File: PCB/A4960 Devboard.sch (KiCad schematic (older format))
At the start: 61 parts, among them IC1 ATMEGA8-AI, P1 CONN_02X03, P2 CONN_01X02, P3 CONN_01X03, P4 CONN_01X03, Q1 Q_NMOS_GDS, Q2 Q_NMOS_GDS, Q3 Q_NMOS_GDS, Q4 Q_NMOS_GDS, Q5 Q_NMOS_GDS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

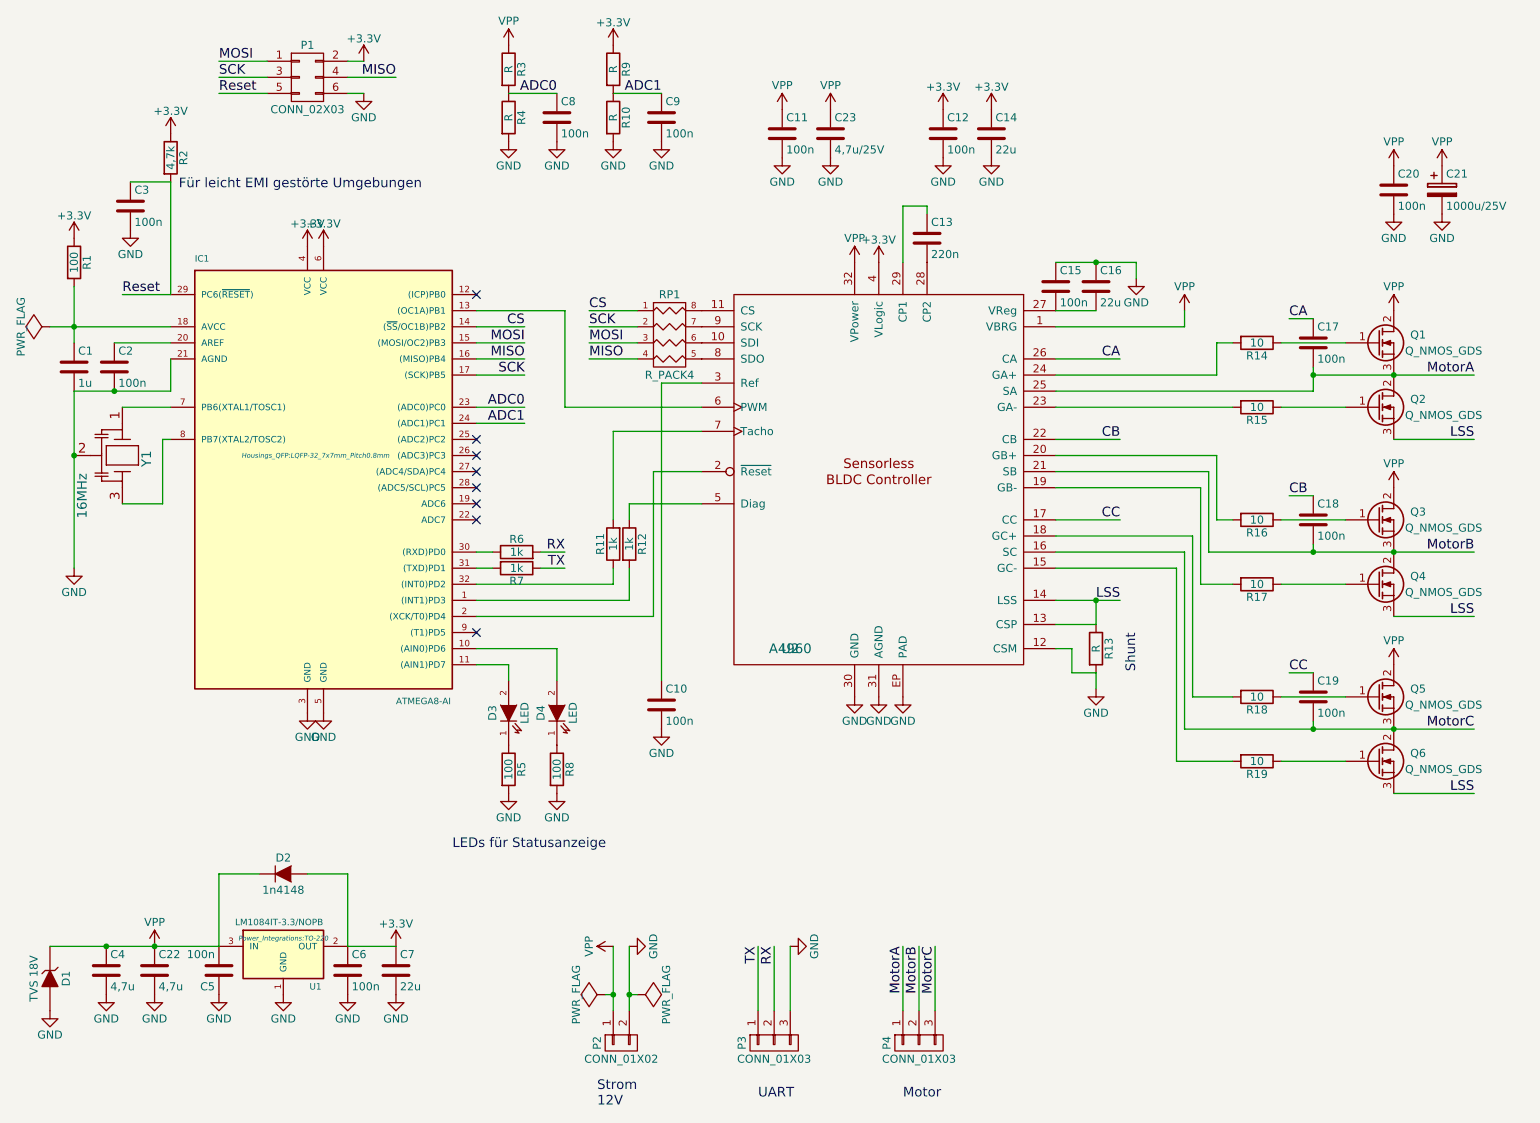
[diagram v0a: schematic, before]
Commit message: Library-Refferenz geändert & Layout: Vcc von 3.3V auf 5V
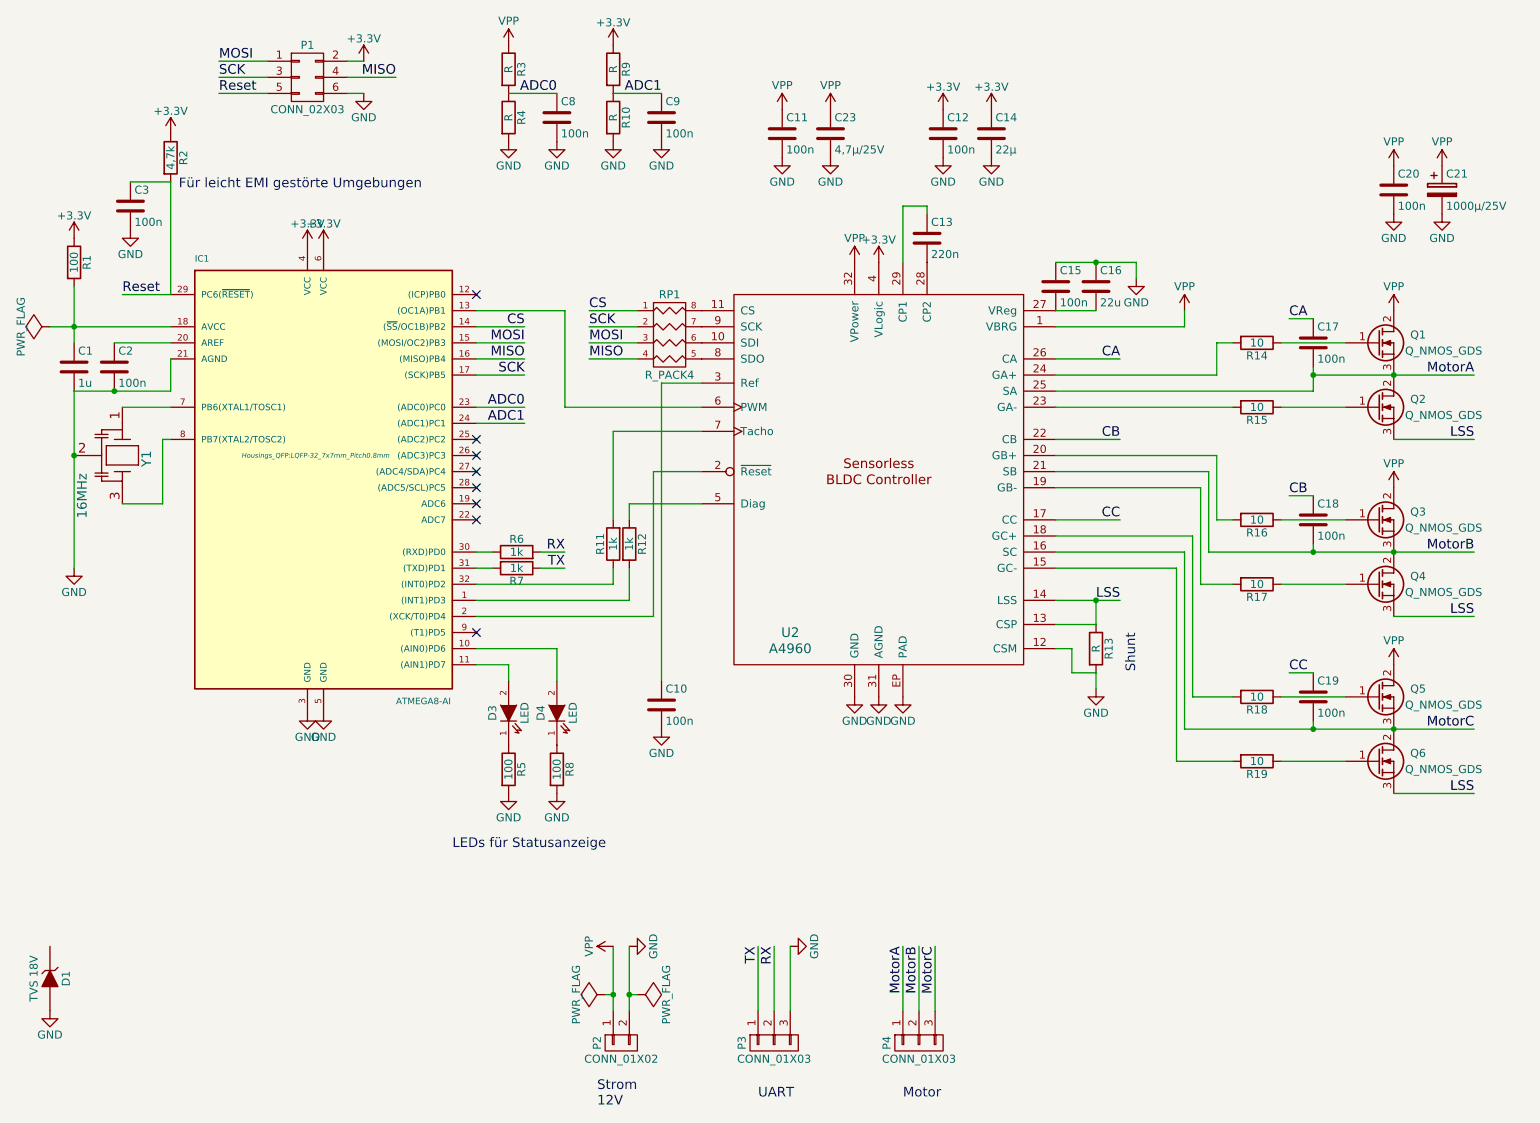
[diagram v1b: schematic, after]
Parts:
- removed C22, C4: 4,7u, Capacitors_SMD:C_1206, symbol C
- removed C5, C6: 100n, Capacitors_SMD:C_0603, symbol C
- removed C7: 22u, Capacitors_SMD:C_1206, symbol C
- removed D2: 1n4148, Diodes_SMD:MiniMELF_Standard, symbol D
- removed U1: LM1084IT-3.3/NOPB, Power_Integrations:TO-220, symbol LM1084IT-3.3/NOPB
- C14: value 22u -> 22µ
- C21: value 1000u/25V -> 1000µ/25V
- C23: value 4,7u/25V -> 4,7µ/25V
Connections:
- net VPP: no longer D1.1 (K)
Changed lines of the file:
@@
 U 1 1 55EC77AA
 P 5950 3550
-F 0 "U2" H 5400 2500 60  0000 C CNN
+F 0 "U2" H 5400 2600 60  0000 C CNN
 F 1 "A4960" H 5400 2500 60  0000 C CNN
 F 2 "Housings_QFP:TQFP-32_7x7mm_Pitch0.8mm" H 5400 2500 60  0001 C CNN
@@
 P 6650 1400
 F 0 "C14" H 6675 1500 50  0000 L CNN
-F 1 "22u" H 6675 1300 50  0000 L CNN
+F 1 "22µ" H 6675 1300 50  0000 L CNN
 F 2 "Capacitors_SMD:C_1206" H 6688 1250 30  0001 C CNN
 F 3 "" H 6650 1400 60  0000 C CNN
@@
 P 9450 1750
 F 0 "C21" H 9475 1850 50  0000 L CNN
-F 1 "1000u/25V" H 9475 1650 50  0000 L CNN
+F 1 "1000µ/25V" H 9475 1650 50  0000 L CNN
 F 2 "" H 9488 1600 30  0001 C CNN
 F 3 "" H 9450 1750 60  0000 C CNN
@@
 LEDs für Statusanzeige
 $Comp
-L LM1084IT-3.3/NOPB U1
-U 1 1 55ECD83D
-P 2250 6500
-F 0 "U1" H 2450 6300 40  0000 C CNN
-F 1 "LM1084IT-3.3/NOPB" H 1950 6700 40  0000 L CNN
-F 2 "Power_Integrations:TO-220" H 2250 6600 30  0000 C CIN
-F 3 "" H 2250 6500 60  0000 C CNN
-	1    2250 6500
-	1    0    0    -1
-$EndComp
-$Comp
-L C C5
-U 1 1 55ECDA89
-P 1850 6600
-F 0 "C5" H 1875 6700 50  0000 L CNN
-F 1 "100n" H 1875 6500 50  0000 L CNN
-F 2 "Capacitors_SMD:C_0603" H 1888 6450 30  0001 C CNN
-F 3 "" H 1850 6600 60  0000 C CNN
-	1    1850 6600
-	-1   0    0    1
-$EndComp
-$Comp
-L C C6
-U 1 1 55ECDC37
-P 2650 6600
-F 0 "C6" H 2675 6700 50  0000 L CNN
-F 1 "100n" H 2675 6500 50  0000 L CNN
-F 2 "Capacitors_SMD:C_0603" H 2688 6450 30  0001 C CNN
-F 3 "" H 2650 6600 60  0000 C CNN
-	1    2650 6600
-	1    0    0    -1
-$EndComp
-$Comp
-L C C7
-U 1 1 55ECDE0F
-P 2950 6600
-F 0 "C7" H 2975 6700 50  0000 L CNN
-F 1 "22u" H 2975 6500 50  0000 L CNN
-F 2 "Capacitors_SMD:C_1206" H 2988 6450 30  0001 C CNN
-F 3 "" H 2950 6600 60  0000 C CNN
-	1    2950 6600
-	1    0    0    -1
-$EndComp
-$Comp
-L GND #PWR040
-U 1 1 55ECE074
-P 1450 6750
-F 0 "#PWR040" H 1450 6500 50  0001 C CNN
-F 1 "GND" H 1450 6600 50  0000 C CNN
-F 2 "" H 1450 6750 60  0000 C CNN
-F 3 "" H 1450 6750 60  0000 C CNN
-	1    1450 6750
-	1    0    0    -1
-$EndComp
-$Comp
-L GND #PWR041
-U 1 1 55ECE11E
-P 1850 6750
-F 0 "#PWR041" H 1850 6500 50  0001 C CNN
-F 1 "GND" H 1850 6600 50  0000 C CNN
-F 2 "" H 1850 6750 60  0000 C CNN
-F 3 "" H 1850 6750 60  0000 C CNN
-	1    1850 6750
-	1    0    0    -1
-$EndComp
-$Comp
-L GND #PWR042
-U 1 1 55ECE1C8
-P 2250 6750
-F 0 "#PWR042" H 2250 6500 50  0001 C CNN
-F 1 "GND" H 2250 6600 50  0000 C CNN
-F 2 "" H 2250 6750 60  0000 C CNN
-F 3 "" H 2250 6750 60  0000 C CNN
-	1    2250 6750
-	1    0    0    -1
-$EndComp
-$Comp
-L GND #PWR043
-U 1 1 55ECE272
-P 2650 6750
-F 0 "#PWR043" H 2650 6500 50  0001 C CNN
-F 1 "GND" H 2650 6600 50  0000 C CNN
-F 2 "" H 2650 6750 60  0000 C CNN
-F 3 "" H 2650 6750 60  0000 C CNN
-	1    2650 6750
-	1    0    0    -1
-$EndComp
-$Comp
-L GND #PWR044
-U 1 1 55ECE31C
-P 2950 6750
-F 0 "#PWR044" H 2950 6500 50  0001 C CNN
-F 1 "GND" H 2950 6600 50  0000 C CNN
-F 2 "" H 2950 6750 60  0000 C CNN
-F 3 "" H 2950 6750 60  0000 C CNN
-	1    2950 6750
-	1    0    0    -1
-$EndComp
-$Comp
 L ZENER D1
 U 1 1 55ECE4C5
@@
 	1    0    0    -1
 $EndComp
-Wire Wire Line
-	800  6450 1850 6450
-Connection ~ 1450 6450
-Wire Wire Line
-	2650 6450 2950 6450
-$Comp
-L +3.3V #PWR046
-U 1 1 55ECE8BB
-P 2950 6450
-F 0 "#PWR046" H 2950 6300 50  0001 C CNN
-F 1 "+3.3V" H 2950 6590 50  0000 C CNN
-F 2 "" H 2950 6450 60  0000 C CNN
-F 3 "" H 2950 6450 60  0000 C CNN
-	1    2950 6450
-	1    0    0    -1
-$EndComp
-$Comp
-L D D2
-U 1 1 55ECE9B8
-P 2250 6000
-F 0 "D2" H 2250 6100 50  0000 C CNN
-F 1 "1n4148" H 2250 5900 50  0000 C CNN
-F 2 "Diodes_SMD:MiniMELF_Standard" H 2250 6000 60  0001 C CNN
-F 3 "" H 2250 6000 60  0000 C CNN
-	1    2250 6000
-	1    0    0    -1
-$EndComp
-Wire Wire Line
-	2400 6000 2650 6000
-Wire Wire Line
-	2650 6000 2650 6450
-Wire Wire Line
-	2100 6000 1850 6000
-Wire Wire Line
-	1850 6000 1850 6450
 $Comp
 L CONN_01X03 P3
@@
 	4400 6450 4400 6850
 $Comp
-L VPP #PWR049
-U 1 1 55ED031C
-P 1450 6450
-F 0 "#PWR049" H 1450 6300 50  0001 C CNN
-F 1 "VPP" H 1450 6600 50  0000 C CNN
-F 2 "" H 1450 6450 60  0000 C CNN
-F 3 "" H 1450 6450 60  0000 C CNN
-	1    1450 6450
-	1    0    0    -1
-$EndComp
-$Comp
 L VPP #PWR050
 U 1 1 55ED0449
@@
 P 5650 1400
 F 0 "C23" H 5675 1500 50  0000 L CNN
-F 1 "4,7u/25V" H 5675 1300 50  0000 L CNN
+F 1 "4,7µ/25V" H 5675 1300 50  0000 L CNN
 F 2 "Capacitors_SMD:C_1206" H 5688 1250 30  0001 C CNN
 F 3 "" H 5650 1400 60  0000 C CNN
@@
 	1    0    0    -1
 $EndComp
-$Comp
-L C C22
-U 1 1 55ED2F02
-P 1450 6600
-F 0 "C22" H 1475 6700 50  0000 L CNN
-F 1 "4,7u" H 1475 6500 50  0000 L CNN
-F 2 "Capacitors_SMD:C_1206" H 1488 6450 30  0001 C CNN
-F 3 "" H 1450 6600 60  0000 C CNN
-F 4 "C1206C475K3RACTU" H 1450 6600 60  0001 C CNN "Herstellername"
-	1    1450 6600
-	1    0    0    -1
-$EndComp
-$Comp
-L C C4
-U 1 1 55ED3212
-P 1150 6600
-F 0 "C4" H 1175 6700 50  0000 L CNN
-F 1 "4,7u" H 1175 6500 50  0000 L CNN
-F 2 "Capacitors_SMD:C_1206" H 1188 6450 30  0001 C CNN
-F 3 "" H 1150 6600 60  0000 C CNN
-F 4 "C1206C475K3RACTU" H 1150 6600 60  0001 C CNN "Herstellername"
-	1    1150 6600
-	1    0    0    -1
-$EndComp
-$Comp
-L GND #PWR057
-U 1 1 55ED32E2
-P 1150 6750
-F 0 "#PWR057" H 1150 6500 50  0001 C CNN
-F 1 "GND" H 1150 6600 50  0000 C CNN
-F 2 "" H 1150 6750 60  0000 C CNN
-F 3 "" H 1150 6750 60  0000 C CNN
-	1    1150 6750
-	1    0    0    -1
-$EndComp
-Connection ~ 1150 6450
 $EndSCHEMATC

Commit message: Änderung der FETs auf Pinnamen GDS
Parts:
- removed Q1, Q2, Q3, Q4, Q5, Q6: Q_NMOS_GDS, Transistors_TO-220:TO-220_Neutral123_Vertical_LargePads, symbol Q_NMOS_GDS
- added Q1, Q2, Q3, Q4, Q5, Q6: Q_NMOS_GDS_old, sven:SO8_WITH_Heatpipes, symbol Q_NMOS_GDS_old
- added R20: 1, Resistors_SMD:R_0805, symbol R
- added U1: LM2931AZ-5.0, toni:SOT223_GND_VO_VI, symbol LM2931AZ-5.0
- C21: footprint (none) -> Capacitors_ThroughHole:C_Radial_D8_L11.5_P3.5
- D1: footprint (none) -> Diodes_SMD:SOD-123
- P1: footprint (none) -> Pin_Headers:Pin_Header_Straight_2x03
- P2: footprint (none) -> Pin_Headers:Pin_Header_Straight_1x02
- P3, P4: footprint (none) -> Pin_Headers:Pin_Header_Straight_1x03
- Y1: footprint (none) -> toni:CerOsc_3,2x1,3
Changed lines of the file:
@@
-$EndComp
-$Comp
-L Q_NMOS_GDS Q1
-U 1 1 55EC7821
-P 9050 2700
-F 0 "Q1" H 9350 2750 50  0000 R CNN
-F 1 "Q_NMOS_GDS" H 9700 2650 50  0000 R CNN
-F 2 "Transistors_TO-220:TO-220_Neutral123_Vertical_LargePads" H 9250 2800 29  0001 C CNN
-F 3 "" H 9050 2700 60  0000 C CNN
-	1    9050 2700
-	1    0    0    -1
-$EndComp
-$Comp
-L Q_NMOS_GDS Q2
-U 1 1 55EC798C
-P 9050 3100
-F 0 "Q2" H 9350 3150 50  0000 R CNN
-F 1 "Q_NMOS_GDS" H 9700 3050 50  0000 R CNN
-F 2 "Transistors_TO-220:TO-220_Neutral123_Vertical_LargePads" H 9250 3200 29  0001 C CNN
-F 3 "" H 9050 3100 60  0000 C CNN
-	1    9050 3100
-	1    0    0    -1
 $EndComp
 $Comp
@@
 $EndComp
 $Comp
-L Q_NMOS_GDS Q3
-U 1 1 55EC85FE
-P 9050 3800
-F 0 "Q3" H 9350 3850 50  0000 R CNN
-F 1 "Q_NMOS_GDS" H 9700 3750 50  0000 R CNN
-F 2 "Transistors_TO-220:TO-220_Neutral123_Vertical_LargePads" H 9250 3900 29  0001 C CNN
-F 3 "" H 9050 3800 60  0000 C CNN
-	1    9050 3800
-	1    0    0    -1
-$EndComp
-$Comp
-L Q_NMOS_GDS Q4
-U 1 1 55EC8604
-P 9050 4200
-F 0 "Q4" H 9350 4250 50  0000 R CNN
-F 1 "Q_NMOS_GDS" H 9700 4150 50  0000 R CNN
-F 2 "Transistors_TO-220:TO-220_Neutral123_Vertical_LargePads" H 9250 4300 29  0001 C CNN
-F 3 "" H 9050 4200 60  0000 C CNN
-	1    9050 4200
-	1    0    0    -1
-$EndComp
-$Comp
 L C C18
 U 1 1 55EC860A
@@
 $EndComp
 $Comp
-L Q_NMOS_GDS Q5
-U 1 1 55EC8730
-P 9050 4900
-F 0 "Q5" H 9350 4950 50  0000 R CNN
-F 1 "Q_NMOS_GDS" H 9700 4850 50  0000 R CNN
-F 2 "Transistors_TO-220:TO-220_Neutral123_Vertical_LargePads" H 9250 5000 29  0001 C CNN
-F 3 "" H 9050 4900 60  0000 C CNN
-	1    9050 4900
-	1    0    0    -1
-$EndComp
-$Comp
-L Q_NMOS_GDS Q6
-U 1 1 55EC8736
-P 9050 5300
-F 0 "Q6" H 9350 5350 50  0000 R CNN
-F 1 "Q_NMOS_GDS" H 9700 5250 50  0000 R CNN
-F 2 "Transistors_TO-220:TO-220_Neutral123_Vertical_LargePads" H 9250 5400 29  0001 C CNN
-F 3 "" H 9050 5300 60  0000 C CNN
-	1    9050 5300
-	1    0    0    -1
-$EndComp
-$Comp
 L C C19
 U 1 1 55EC873C
@@
 F 0 "C21" H 9475 1850 50  0000 L CNN
 F 1 "1000µ/25V" H 9475 1650 50  0000 L CNN
-F 2 "" H 9488 1600 30  0001 C CNN
+F 2 "Capacitors_ThroughHole:C_Radial_D8_L11.5_P3.5" H 9488 1600 30  0001 C CNN
 F 3 "" H 9450 1750 60  0000 C CNN
 	1    9450 1750
@@
 F 0 "Y1" H 1220 3600 60  0000 C CNN
 F 1 "16MHz" H 1450 3200 60  0000 C CNN
-F 2 "" H 1200 3400 60  0001 C CNN
+F 2 "toni:CerOsc_3,2x1,3" H 1200 3400 60  0001 C CNN
 F 3 "" H 1200 3400 60  0000 C CNN
 	1    1200 3400
@@
 F 0 "P1" H 2400 1250 50  0000 C CNN
 F 1 "CONN_02X03" H 2400 850 50  0000 C CNN
-F 2 "" H 2400 -150 60  0001 C CNN
+F 2 "Pin_Headers:Pin_Header_Straight_2x03" H 2400 -150 60  0001 C CNN
 F 3 "" H 2400 -150 60  0000 C CNN
 	1    2400 1050
@@
 F 0 "D1" H 800 6750 50  0000 C CNN
 F 1 "TVS 18V" H 800 6550 50  0000 C CNN
-F 2 "" H 800 6650 60  0001 C CNN
+F 2 "Diodes_SMD:SOD-123" H 800 6650 60  0001 C CNN
 F 3 "" H 800 6650 60  0000 C CNN
 	1    800  6650
@@
 F 0 "P3" H 5300 7250 50  0000 C CNN
 F 1 "CONN_01X03" V 5400 7050 50  0000 C CNN
-F 2 "" H 5300 7050 60  0001 C CNN
+F 2 "Pin_Headers:Pin_Header_Straight_1x03" H 5300 7050 60  0001 C CNN
 F 3 "" H 5300 7050 60  0000 C CNN
 	1    5300 7050
@@
 F 0 "P2" H 4350 7200 50  0000 C CNN
 F 1 "CONN_01X02" V 4450 7050 50  0000 C CNN
-F 2 "" H 4350 7050 60  0001 C CNN
+F 2 "Pin_Headers:Pin_Header_Straight_1x02" H 4350 7050 60  0001 C CNN
 F 3 "" H 4350 7050 60  0000 C CNN
 	1    4350 7050
@@
 F 0 "P4" H 6200 7250 50  0000 C CNN
 F 1 "CONN_01X03" V 6300 7050 50  0000 C CNN
-F 2 "" H 6200 7050 60  0001 C CNN
+F 2 "Pin_Headers:Pin_Header_Straight_1x03" H 6200 7050 60  0001 C CNN
 F 3 "" H 6200 7050 60  0000 C CNN
 	1    6200 7050
@@
 	1    0    0    -1
 $EndComp
+$Comp
+L LM2931AZ-5.0 U1
+U 1 1 5653AFAA
+P 2400 6725
+F 0 "U1" H 2400 6975 40  0000 C CNN
+F 1 "LM2931AZ-5.0" H 2400 6925 40  0000 C CNN
+F 2 "toni:SOT223_GND_VO_VI" H 2400 6825 35  0001 C CIN
+F 3 "" H 2400 6725 60  0000 C CNN
+	1    2400 6725
+	1    0    0    -1
+$EndComp
+$Comp
+L +3.3V #PWR050
+U 1 1 5653B466
+P 2800 6675
+F 0 "#PWR050" H 2800 6525 50  0001 C CNN
+F 1 "+3.3V" H 2800 6815 50  0000 C CNN
+F 2 "" H 2800 6675 60  0000 C CNN
+F 3 "" H 2800 6675 60  0000 C CNN
+	1    2800 6675
+	1    0    0    -1
+$EndComp
+$Comp
+L GND #PWR051
+U 1 1 5653BE8A
+P 2400 6975
+F 0 "#PWR051" H 2400 6725 50  0001 C CNN
+F 1 "GND" H 2400 6825 50  0000 C CNN
+F 2 "" H 2400 6975 60  0000 C CNN
+F 3 "" H 2400 6975 60  0000 C CNN
+	1    2400 6975
+	1    0    0    -1
+$EndComp
+$Comp
+L VPP #PWR052
+U 1 1 5653BF3A
+P 1700 6675
+F 0 "#PWR052" H 1700 6525 50  0001 C CNN
+F 1 "VPP" H 1700 6825 50  0000 C CNN
+F 2 "" H 1700 6675 60  0000 C CNN
+F 3 "" H 1700 6675 60  0000 C CNN
+	1    1700 6675
+	0    -1   -1   0
+$EndComp
+$Comp
+L R R20
+U 1 1 5653BFEC
+P 1850 6675
+F 0 "R20" V 1930 6675 50  0000 C CNN
+F 1 "1" V 1850 6675 50  0000 C CNN
+F 2 "Resistors_SMD:R_0805" V 1780 6675 30  0001 C CNN
+F 3 "" H 1850 6675 30  0000 C CNN
+	1    1850 6675
+	0    1    1    0
+$EndComp
+$Comp
+L VPP #PWR053
+U 1 1 5653D0D0
+P 800 6450
+F 0 "#PWR053" H 800 6300 50  0001 C CNN
+F 1 "VPP" H 800 6600 50  0000 C CNN
+F 2 "" H 800 6450 60  0000 C CNN
+F 3 "" H 800 6450 60  0000 C CNN
+	1    800  6450
+	1    0    0    -1
+$EndComp
+$Comp
+L Q_NMOS_GDS_old Q1
+U 1 1 56540E55
+P 9050 2700
+F 0 "Q1" H 9350 2750 50  0000 R CNN
+F 1 "Q_NMOS_GDS_old" H 9700 2650 50  0000 R CNN
+F 2 "sven:SO8_WITH_Heatpipes" H 9250 2800 29  0001 C CNN
+F 3 "" H 9050 2700 60  0000 C CNN
+	1    9050 2700
+	1    0    0    -1
+$EndComp
+$Comp
+L Q_NMOS_GDS_old Q2
+U 1 1 565412E8
+P 9050 3100
+F 0 "Q2" H 9350 3150 50  0000 R CNN
+F 1 "Q_NMOS_GDS_old" H 9700 3050 50  0000 R CNN
+F 2 "sven:SO8_WITH_Heatpipes" H 9250 3200 29  0001 C CNN
+F 3 "" H 9050 3100 60  0000 C CNN
+	1    9050 3100
+	1    0    0    -1
+$EndComp
+$Comp
+L Q_NMOS_GDS_old Q3
+U 1 1 56541494
+P 9050 3800
+F 0 "Q3" H 9350 3850 50  0000 R CNN
+F 1 "Q_NMOS_GDS_old" H 9700 3750 50  0000 R CNN
+F 2 "sven:SO8_WITH_Heatpipes" H 9250 3900 29  0001 C CNN
+F 3 "" H 9050 3800 60  0000 C CNN
+	1    9050 3800
+	1    0    0    -1
+$EndComp
+$Comp
+L Q_NMOS_GDS_old Q4
+U 1 1 565416B9
+P 9050 4200
+F 0 "Q4" H 9350 4250 50  0000 R CNN
+F 1 "Q_NMOS_GDS_old" H 9700 4150 50  0000 R CNN
+F 2 "sven:SO8_WITH_Heatpipes" H 9250 4300 29  0001 C CNN
+F 3 "" H 9050 4200 60  0000 C CNN
+	1    9050 4200
+	1    0    0    -1
+$EndComp
+$Comp
+L Q_NMOS_GDS_old Q5
+U 1 1 5654183F
+P 9050 4900
+F 0 "Q5" H 9350 4950 50  0000 R CNN
+F 1 "Q_NMOS_GDS_old" H 9700 4850 50  0000 R CNN
+F 2 "sven:SO8_WITH_Heatpipes" H 9250 5000 29  0001 C CNN
+F 3 "" H 9050 4900 60  0000 C CNN
+	1    9050 4900
+	1    0    0    -1
+$EndComp
+$Comp
+L Q_NMOS_GDS_old Q6
+U 1 1 5654192E
+P 9050 5300
+F 0 "Q6" H 9350 5350 50  0000 R CNN
+F 1 "Q_NMOS_GDS_old" H 9700 5250 50  0000 R CNN
+F 2 "sven:SO8_WITH_Heatpipes" H 9250 5400 29  0001 C CNN
+F 3 "" H 9050 5300 60  0000 C CNN
+	1    9050 5300
+	1    0    0    -1
+$EndComp
